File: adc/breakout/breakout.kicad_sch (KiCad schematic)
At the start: 70 parts, among them J1 Conn_01x05_Pin, J2 Conn_01x05_Pin, J3 Conn_01x03_Pin, J4 Conn_01x06_Pin, U1 ESD5344D-TP, U2 ADS1261IRHBR, U3 ESD5344D-TP, U4 ESD5344D-TP, U5 TPS7A2050PDBVR, U6 TPS61252DSG, U7 XC6206P332MR

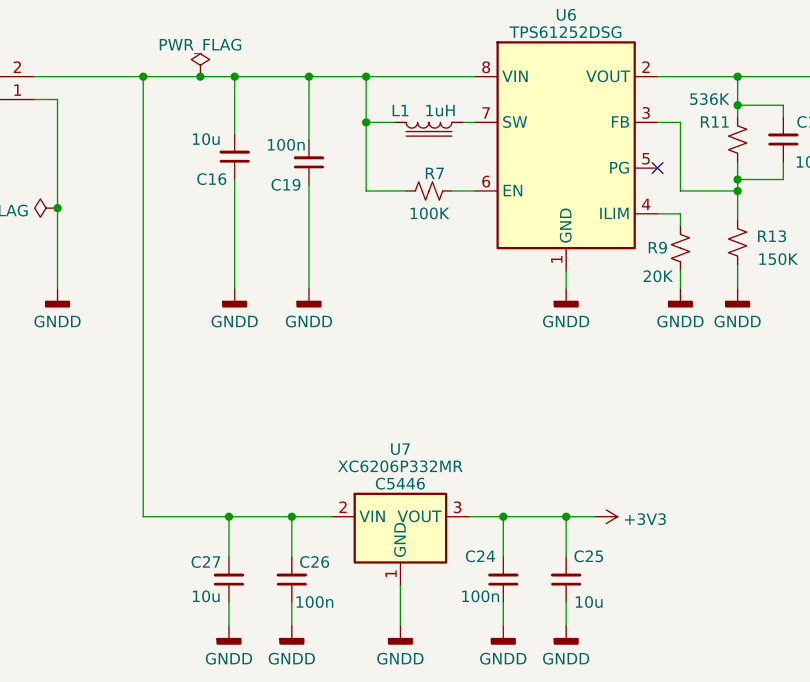
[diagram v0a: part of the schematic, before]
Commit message: Fixed pinout of 3.3V regulator. Final touches.
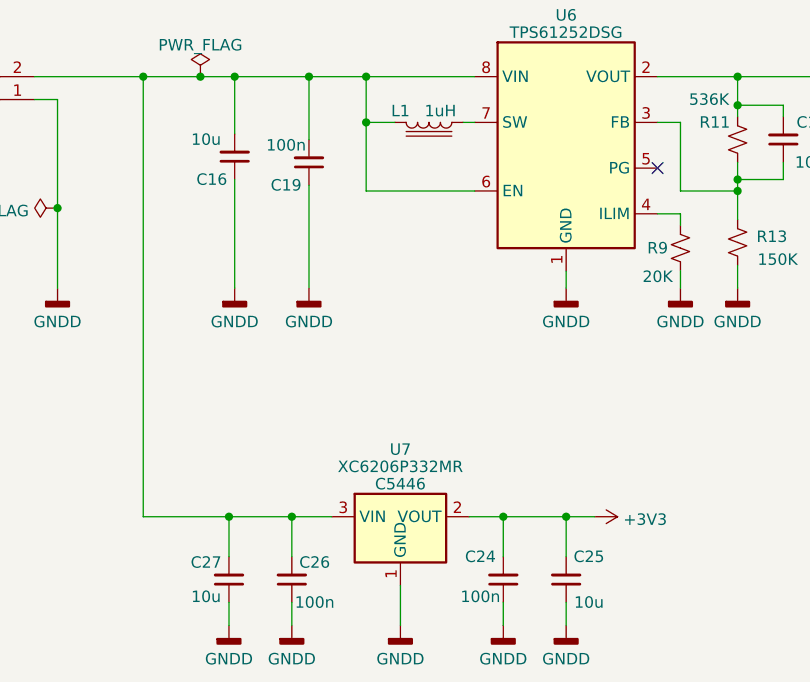
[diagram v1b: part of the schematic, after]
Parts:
- removed R7: 100K, Resistor_SMD:R_0402_1005Metric, symbol Device:R_Small_US
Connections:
- net +3V3: now also U7.2 (VOUT); no longer U7.3 (VOUT)
- net at C16.2, C19.2, C26.2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: now also U6.6 (EN), U7.3 (VIN); no longer U7.2 (VIN)
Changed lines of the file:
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@@
-    (stroke (width 0) (type default))
-  )
-  (wire (pts (xy 88.9 156.21) (xy 84.455 156.21))
     (stroke (width 0) (type default))
   )
@@
     (stroke (width 0) (type default))
   )
-  (wire (pts (xy 93.98 156.21) (xy 96.52 156.21))
+  (wire (pts (xy 84.455 156.21) (xy 96.52 156.21))
     (stroke (width 0) (type default))
   )
@@
         )
       )
-    )
-  )
-  (symbol (lib_id "Device:R_Small_US") (at 91.44 156.21 270) (unit 1)
-    (in_bom yes) (on_board yes) (dnp no)
-    (property "Reference" "R7" (at 92.075 154.305 90)
-      (effects (font (size 1.27 1.27)))
-    )
-    (property "Value" "100K" (at 91.44 158.75 90)
-      (effects (font (size 1.27 1.27)))
-    )
-    (property "Footprint" "Resistor_SMD:R_0402_1005Metric" (at 91.44 156.21 0)
-      (effects (font (size 1.27 1.27)) hide)
-    )
-    (property "Datasheet" "~" (at 91.44 156.21 0)
-      (effects (font (size 1.27 1.27)) hide)
-    )
-    (property "LCSC" "C25741" (at 91.44 156.21 0)
-      (effects (font (size 1.27 1.27)) hide)
-    )
-    (pin "1")
-    (pin "2")
-    (instances
-      (project "breakout"
-        (path "/20ea543f-efab-45c2-9faf-6629ee17c3db"
-          (reference "R7") (unit 1)
-        )
-      )

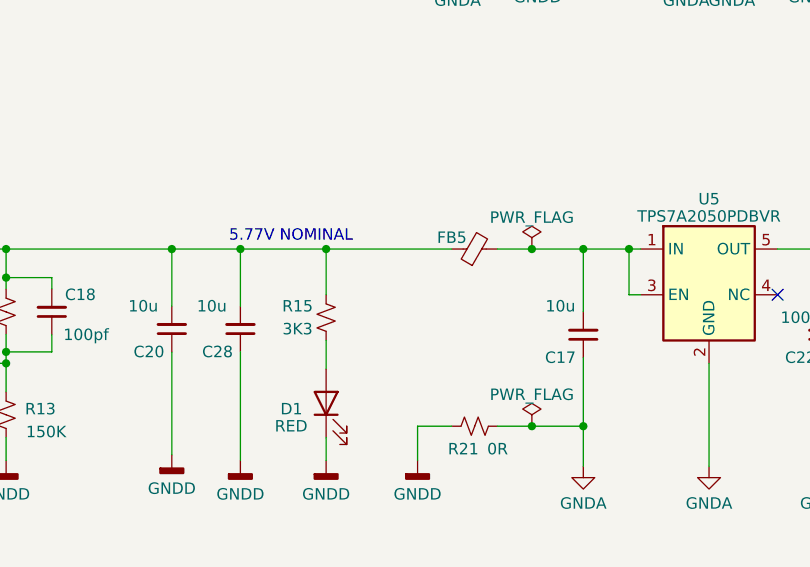
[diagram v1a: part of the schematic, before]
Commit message: Fixed LCSC part number of LED resistor.
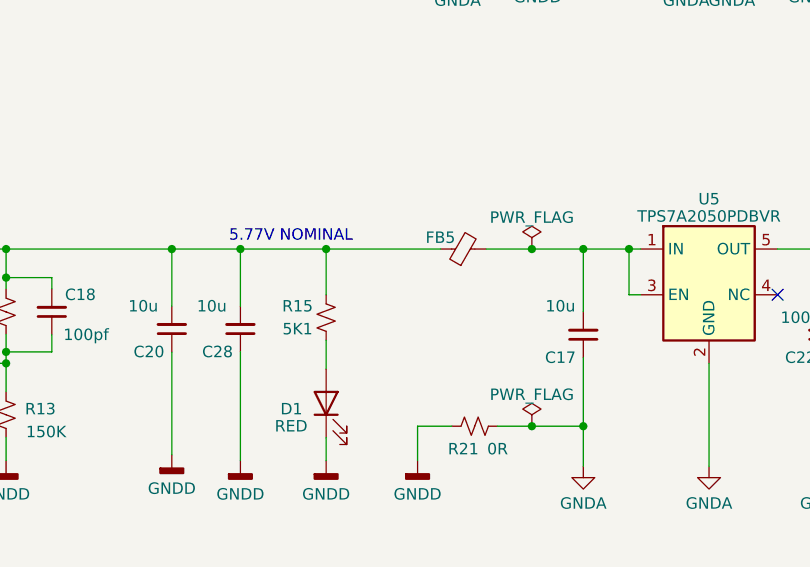
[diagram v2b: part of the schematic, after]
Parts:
- R15: value 3K3 -> 5K1; LCSC C25882 -> C25905
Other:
- moved on the sheet: FB5
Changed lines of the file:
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@@
     (stroke (width 0) (type default))
   )
-  (wire (pts (xy 180.34 143.51) (xy 184.15 143.51))
+  (wire (pts (xy 179.07 143.51) (xy 184.15 143.51))
     (stroke (width 0) (type default))
   )
@@
     (stroke (width 0) (type default))
   )
-  (wire (pts (xy 161.29 143.51) (xy 175.26 143.51))
+  (wire (pts (xy 161.29 143.51) (xy 173.99 143.51))
     (stroke (width 0) (type default))
   )
@@
     )
   )
-  (symbol (lib_id "Device:FerriteBead_Small") (at 177.8 143.51 90) (unit 1)
-    (in_bom yes) (on_board yes) (dnp no)
-    (property "Reference" "FB5" (at 175.26 142.24 90)
-      (effects (font (size 1.27 1.27)))
-    )
-    (property "Value" "Ferrite Bead" (at 177.7619 140.7193 90)
-      (effects (font (size 1.27 1.27)) hide)
-    )
-    (property "Footprint" "Inductor_SMD:L_0805_2012Metric" (at 177.8 145.288 90)
-      (effects (font (size 1.27 1.27)) hide)
-    )
-    (property "Datasheet" "~" (at 177.8 143.51 0)
-      (effects (font (size 1.27 1.27)) hide)
-    )
-    (property "LCSC" "C1017" (at 177.8 143.51 0)
+  (symbol (lib_id "Device:FerriteBead_Small") (at 176.53 143.51 90) (unit 1)
+    (in_bom yes) (on_board yes) (dnp no)
+    (property "Reference" "FB5" (at 173.99 142.24 90)
+      (effects (font (size 1.27 1.27)))
+    )
+    (property "Value" "Ferrite Bead" (at 176.4919 140.7193 90)
+      (effects (font (size 1.27 1.27)) hide)
+    )
+    (property "Footprint" "Inductor_SMD:L_0805_2012Metric" (at 176.53 145.288 90)
+      (effects (font (size 1.27 1.27)) hide)
+    )
+    (property "Datasheet" "~" (at 176.53 143.51 0)
+      (effects (font (size 1.27 1.27)) hide)
+    )
+    (property "LCSC" "C1017" (at 176.53 143.51 0)
       (effects (font (size 1.27 1.27)) hide)
     )
@@
       (effects (font (size 1.27 1.27)))
     )
-    (property "Value" "3K3" (at 158.115 152.4 0)
+    (property "Value" "5K1" (at 158.115 152.4 0)
       (effects (font (size 1.27 1.27)))
     )
@@
       (effects (font (size 1.27 1.27)) hide)
     )
-    (property "LCSC" "C25882" (at 161.29 151.13 0)
-      (effects (font (size 1.27 1.27)) hide)
-    )
+    (property "LCSC" "C25905" (at 161.29 151.13 0)
+      (effects (font (size 1.27 1.27)) hide)
+    )

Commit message: Removed yet another reference id from the top silkscreen.
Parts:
- U2: footprint RHB0032E -> breakout:RHB0032E
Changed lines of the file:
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@@
       (effects (font (size 1.524 1.524)))
     )
-    (property "Footprint" "RHB0032E" (at 177.165 101.6 0)
+    (property "Footprint" "breakout:RHB0032E" (at 177.165 101.6 0)
       (effects (font (size 1.27 1.27) italic) hide)
     )

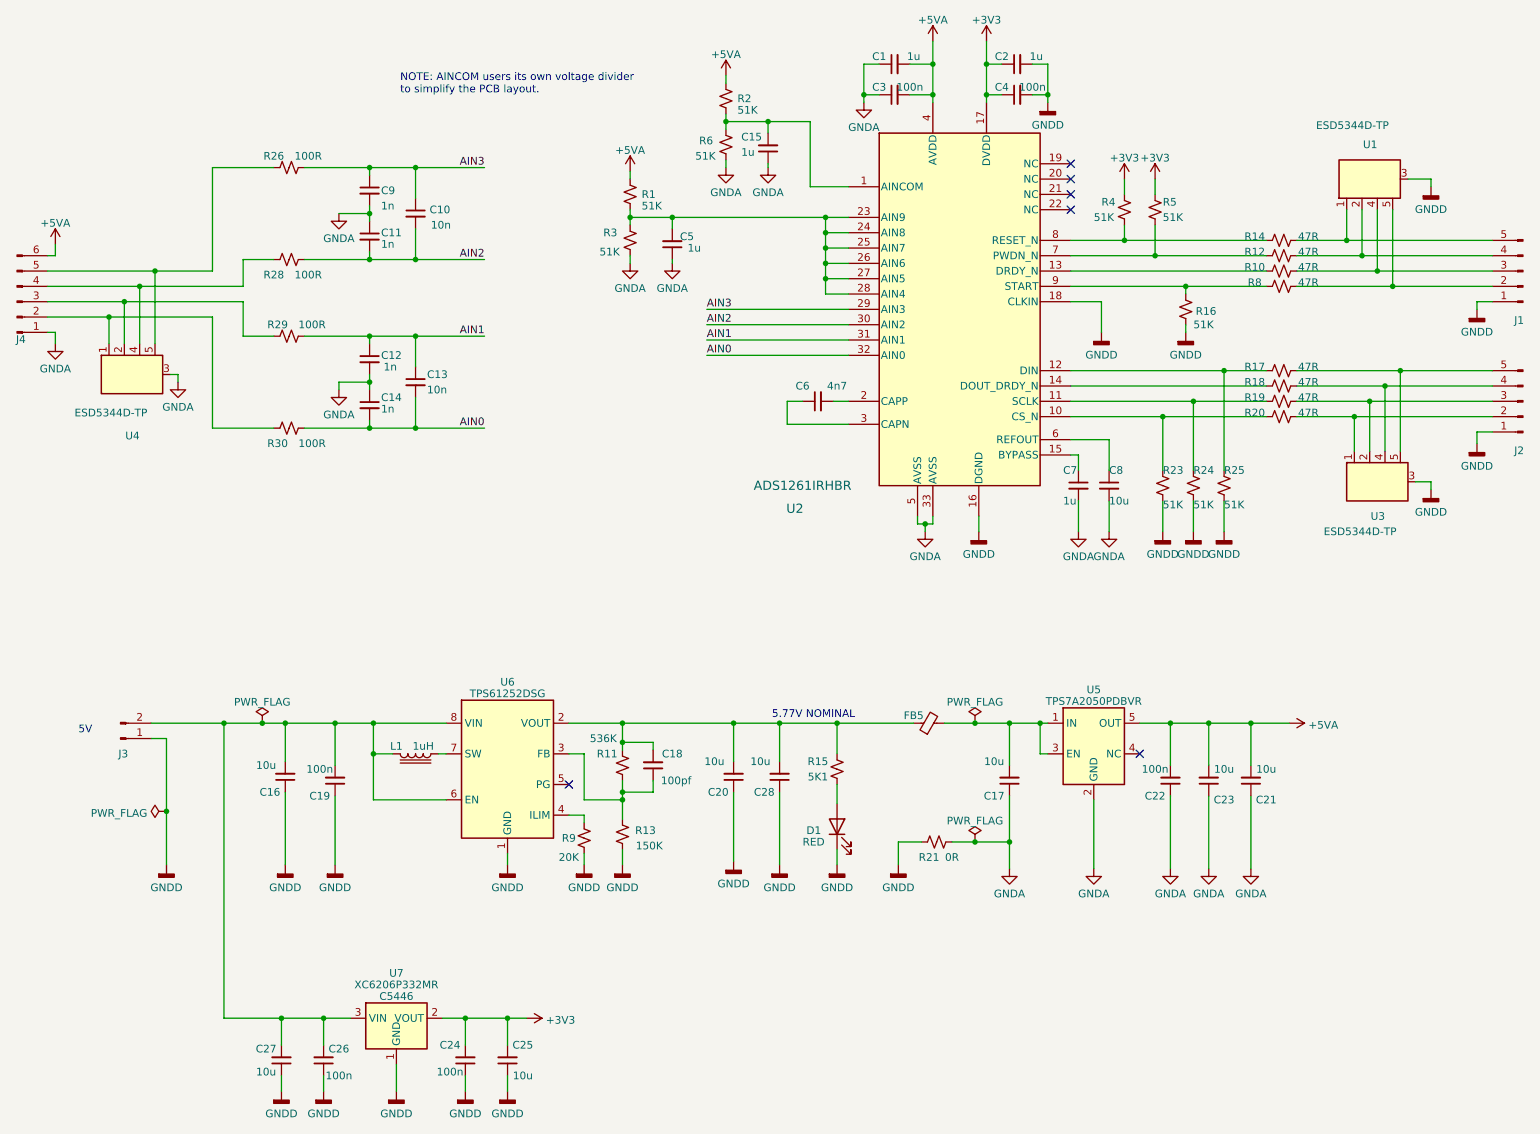
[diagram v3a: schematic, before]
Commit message: Changed dc/dc/ voltage divider to JLCPCB Basic resistor values.
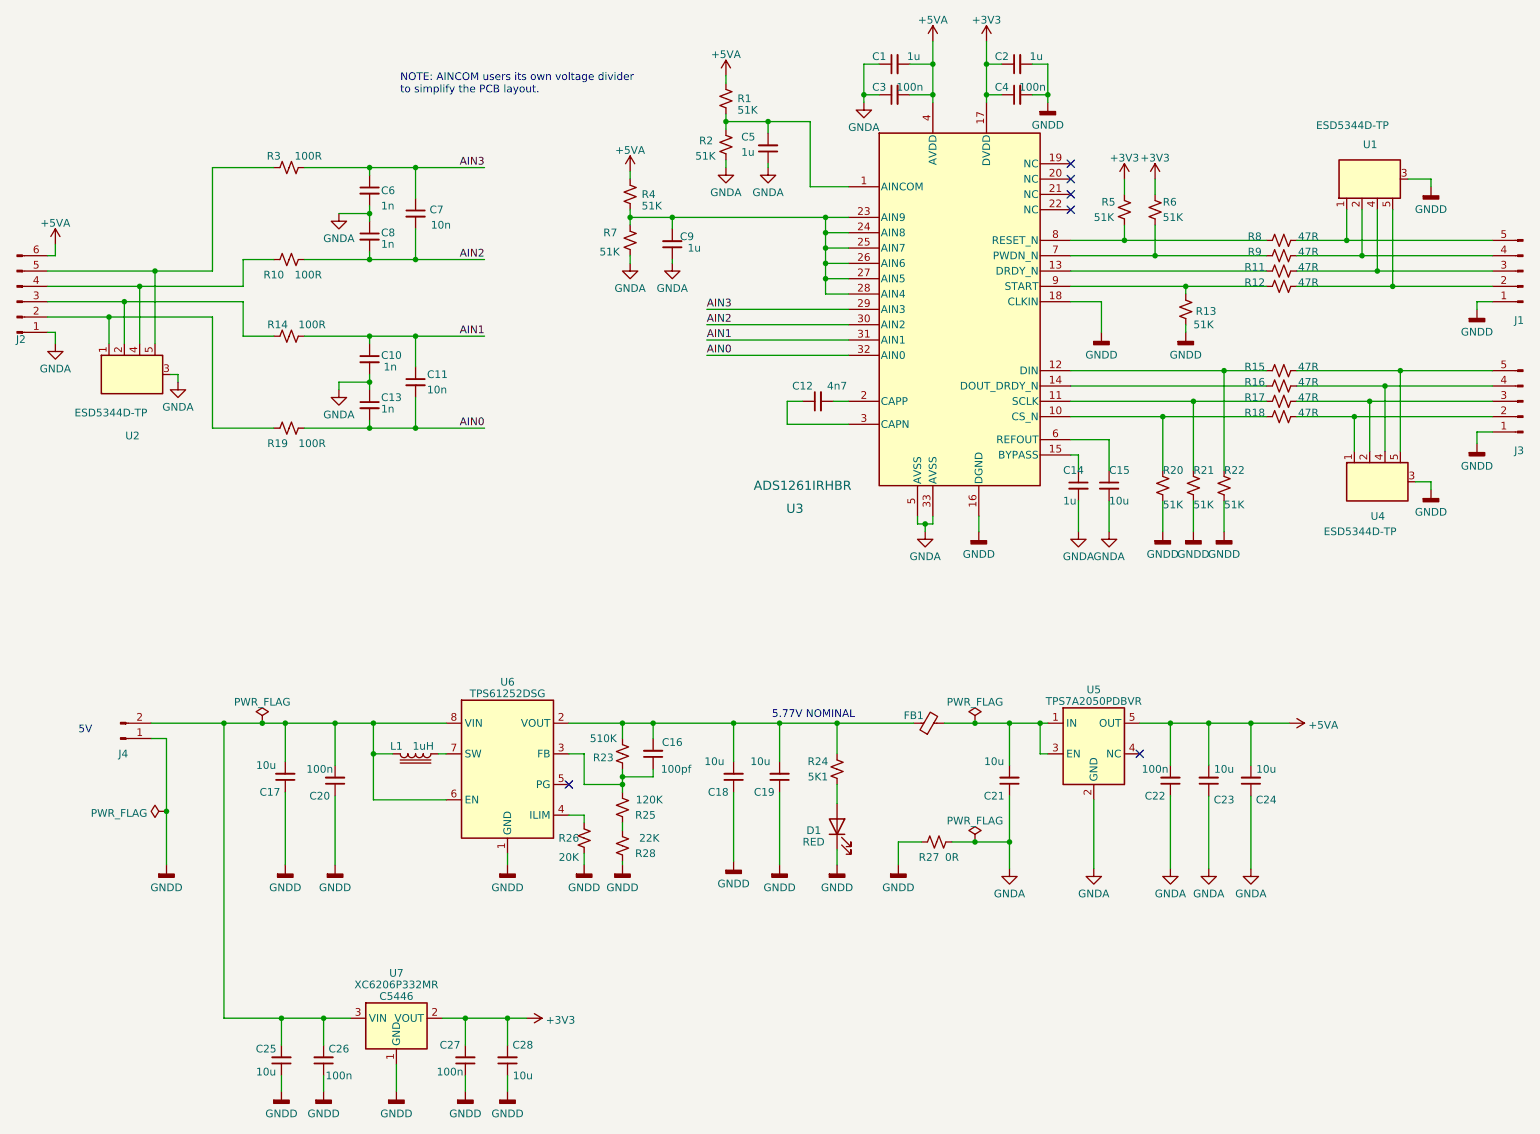
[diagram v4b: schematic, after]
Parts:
- added R28: 22K, Resistor_SMD:R_0402_1005Metric, symbol Device:R_Small_US
- R23: renamed from R11; value 536K -> 510K; LCSC C327337 -> C11616
- R25: renamed from R13; value 150K -> 120K; LCSC C25755 -> C25750
- renumbered C12 to C10, C13 to C11, C6 to C12, C14 to C13, C7 to C14, C8 to C15, C18 to C16, C16 to C17, C20 to C18, C28 to C19, C19 to C20, C17 to C21, C21 to C24, C27 to C25, C24 to C27, C25 to C28, C15 to C5, C9 to C6, C10 to C7, C11 to C8, C5 to C9, FB5 to FB1, J4 to J2, J2 to J3, J3 to J4, R2 to R1, R28 to R10, R10 to R11, R8 to R12, R16 to R13, R29 to R14, R17 to R15, R18 to R16, R19 to R17, R20 to R18, R30 to R19, R6 to R2, R23 to R20, R24 to R21, R25 to R22, R15 to R24, R9 to R26, R21 to R27, R26 to R3, R1 to R4, R4 to R5, R5 to R6, R3 to R7, R14 to R8, R12 to R9, U4 to U2, U2 to U3, U3 to U4
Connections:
- net GNDD: now also R28.1; no longer R25.2
- net at C16.1, R23.2, U6.3 (FB): now also R25.2; no longer R25.1
- new net: R25.1, R28.2
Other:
- moved on the sheet: C16, R23, R25

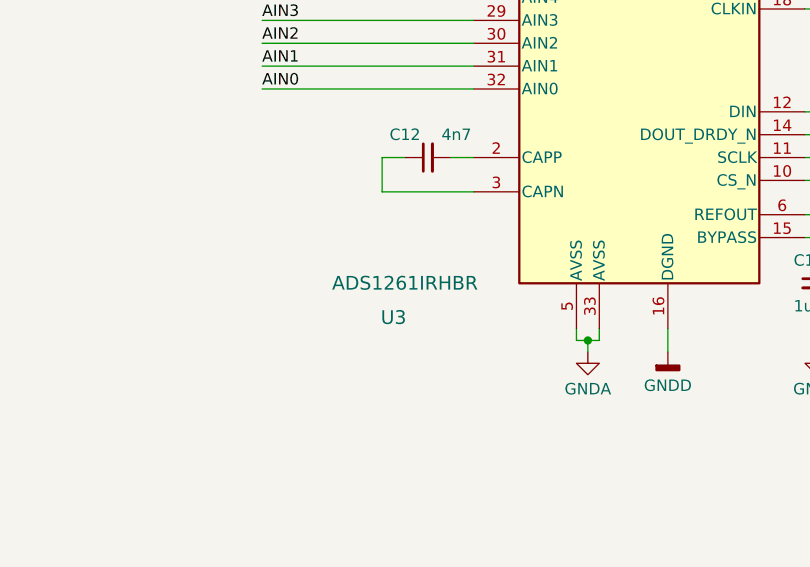
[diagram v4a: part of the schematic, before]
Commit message: Fixed the ADS1261 part value to ADS1261B.
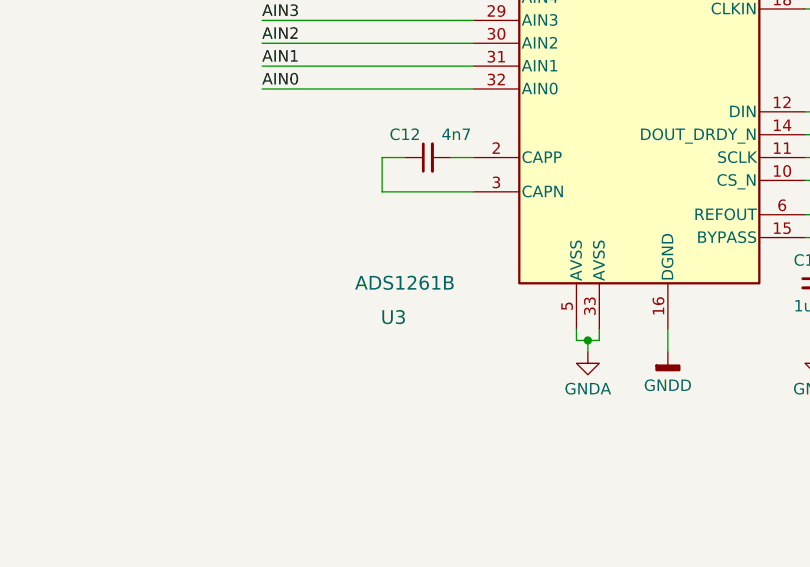
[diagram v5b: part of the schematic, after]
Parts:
- U3: value ADS1261IRHBR -> ADS1261B
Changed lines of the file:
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@@
       (effects (font (size 1.524 1.524)))
     )
-    (property "Value" "ADS1261IRHBR" (at 155.575 104.14 0)
+    (property "Value" "ADS1261B" (at 155.575 104.14 0)
       (effects (font (size 1.524 1.524)))
     )

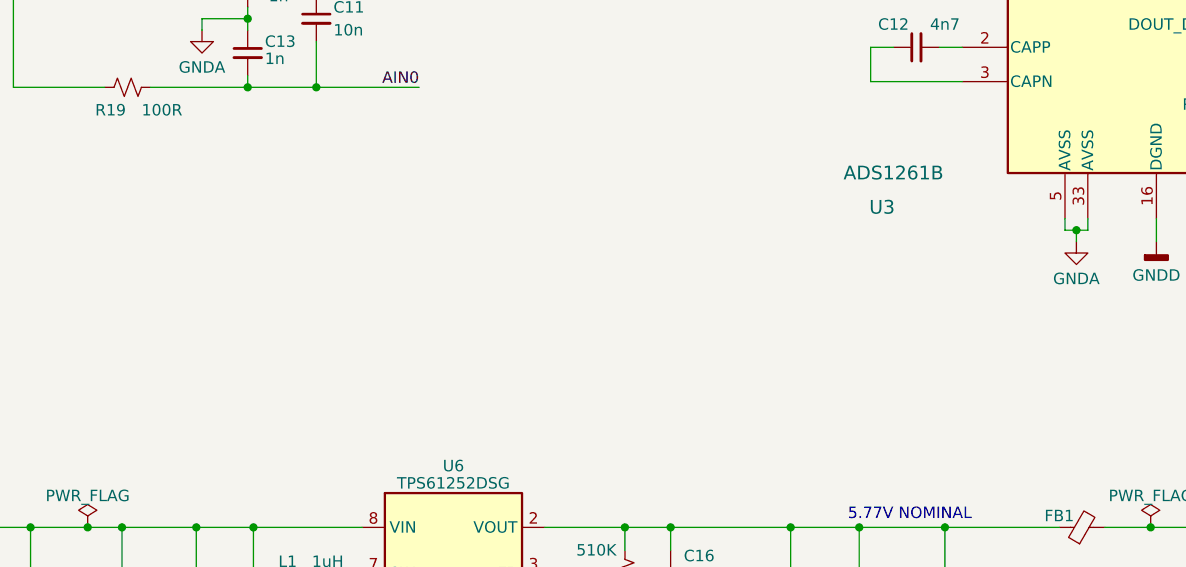
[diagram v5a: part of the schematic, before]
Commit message: Added a TODO to the ADC breakout schematic..
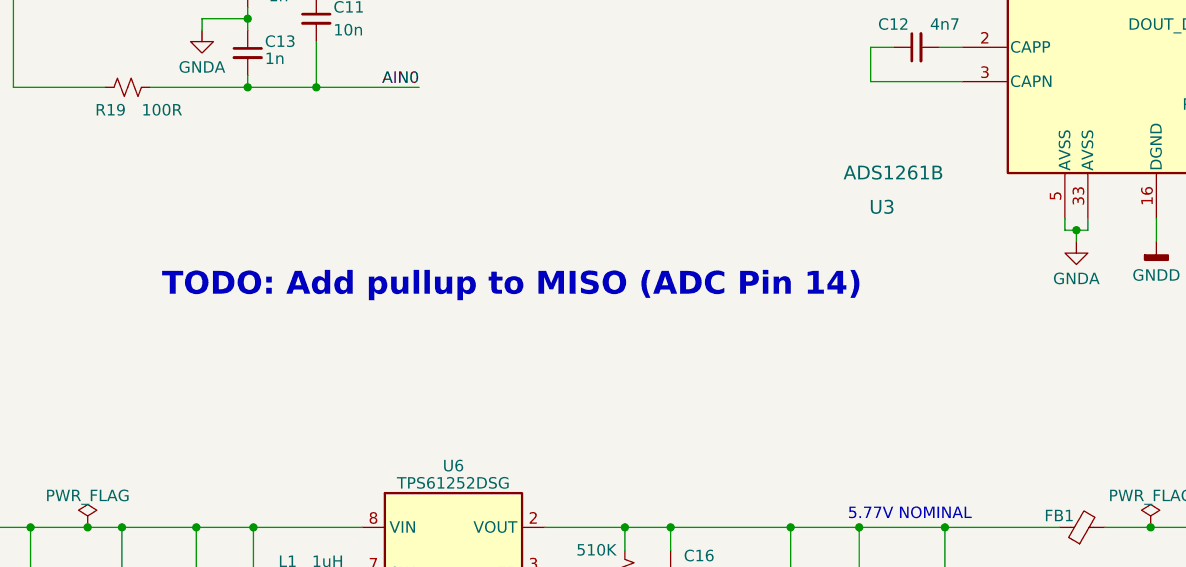
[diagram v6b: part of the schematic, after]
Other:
- note added: "TODO: Add pullup to MISO (ADC Pin 14)"
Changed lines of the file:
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@@
     (stroke (width 0) (type default))
+  )
+  (text "TODO: Add pullup to MISO (ADC Pin 14)" (at 74.295 118.11 0)
+    (effects (font (size 2.54 2.54) (thickness 0.508) bold (color 255 0 0 1)) (justify left bottom))
   )
   (text "NOTE: AINCOM users its own voltage divider\nto simplify the PCB layout."
